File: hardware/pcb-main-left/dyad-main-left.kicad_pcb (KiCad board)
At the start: 2 copper layers, 149 x 120.7 mm, 129 parts, among them SW1 SW_Push, SW10 SW_Push, SW11 SW_Push, SW12 SW_Push, SW13 SW_Push, SW14 SW_Push, SW15 SW_Push, SW16 SW_Push, SW17 SW_Push, SW18 SW_Push, SW19 SW_Push, SW2 SW_Push, SW20 SW_Push, SW21 SW_Push, SW22 SW_Push, SW23 SW_Push, SW24 SW_Push, SW25 SW_Push, SW26 SW_Push, SW27 SW_Push, SW28 SW_Push, SW29 SW_Push, SW3 SW_Push, SW30 SW_Push, SW31 SW_Push, SW32 SW_Push, SW4 SW_Push, SW5 SW_Push, SW6 SW_Push, SW7 SW_Push, SW8 SW_Push, SW9 SW_Push

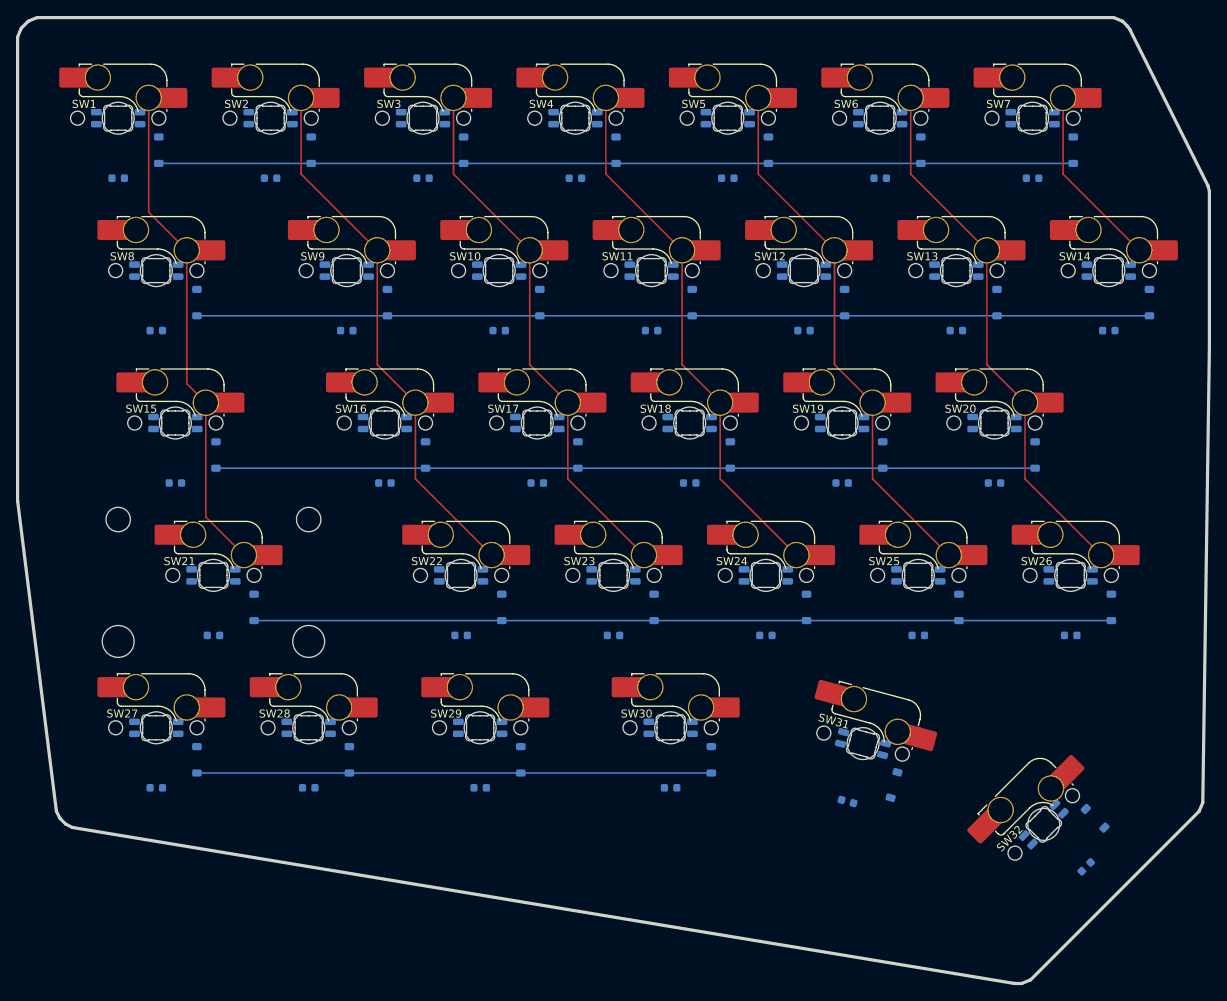
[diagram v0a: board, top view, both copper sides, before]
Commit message: Place switches on the back so hotswap sockets are on the underside
Caught in review: the sockets were on the same side as the switches.

marbastlib's hotswap footprint carries its socket pads on F.Cu and draws
its pin holes mirrored -- it is drawn as seen from underneath and must be
placed on the back. kbplacer defaults to front, so the sockets landed on
the switch side. Fixed with -s "SW{} 0 BACK"; stabilizers follow (they are
purely mechanical NPTH and X-symmetric, so flipping is a no-op for them).

Now every component is on the underside and switches insert from the top,
as a hotswap board should be. Verified: SW1's hotswap SMD pads are on
B.Cu, and the pin1->pin2 vector is (-6.35, 2.54), matching KiCad's stock
SW_Cherry_MX_1.00u_PCB. Absolute pad coordinates are not comparable
between the two libraries -- marbastlib's origin is the switch centre,
KiCad's is pin 1 -- so the vector is the valid test. An earlier claim in
this session that the geometry was mirrored wrongly was based on that bad
comparison and was itself wrong.

Also drops switch-to-diode routing failures, which were "no common layers
found" precisely because front-only SMD pads could not reach back-side
diodes.

DRC now runs and the boards are clearly a placement scaffold, not a
finished layout. Left: 1151 violations, 220 unconnected. Specific causes,
for the next pass:

- 128 hole_clearance: LEDs sit at the switch centre, 0.121 mm from the MX
  centre-post NPTH. The centre is where marbastlib puts its own combined
  MX+WS2812 footprint, but SK6812MINI-E is larger and fouls the post. LED
  offset needs rework.
- 128 copper_edge_clearance: the reverse-mount LED footprint's own cutout
  sits 0.35 mm from its pads against a 0.5 mm board rule. A board-setup
  constraint to relax, not a placement error.
- 192 shorting_items: diode pads overlapping switch through-holes after
  the flip, plus hotswap SMD pads left with no net, which points at an
  incomplete schematic-to-PCB netlist sync.
- Silk overlaps a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
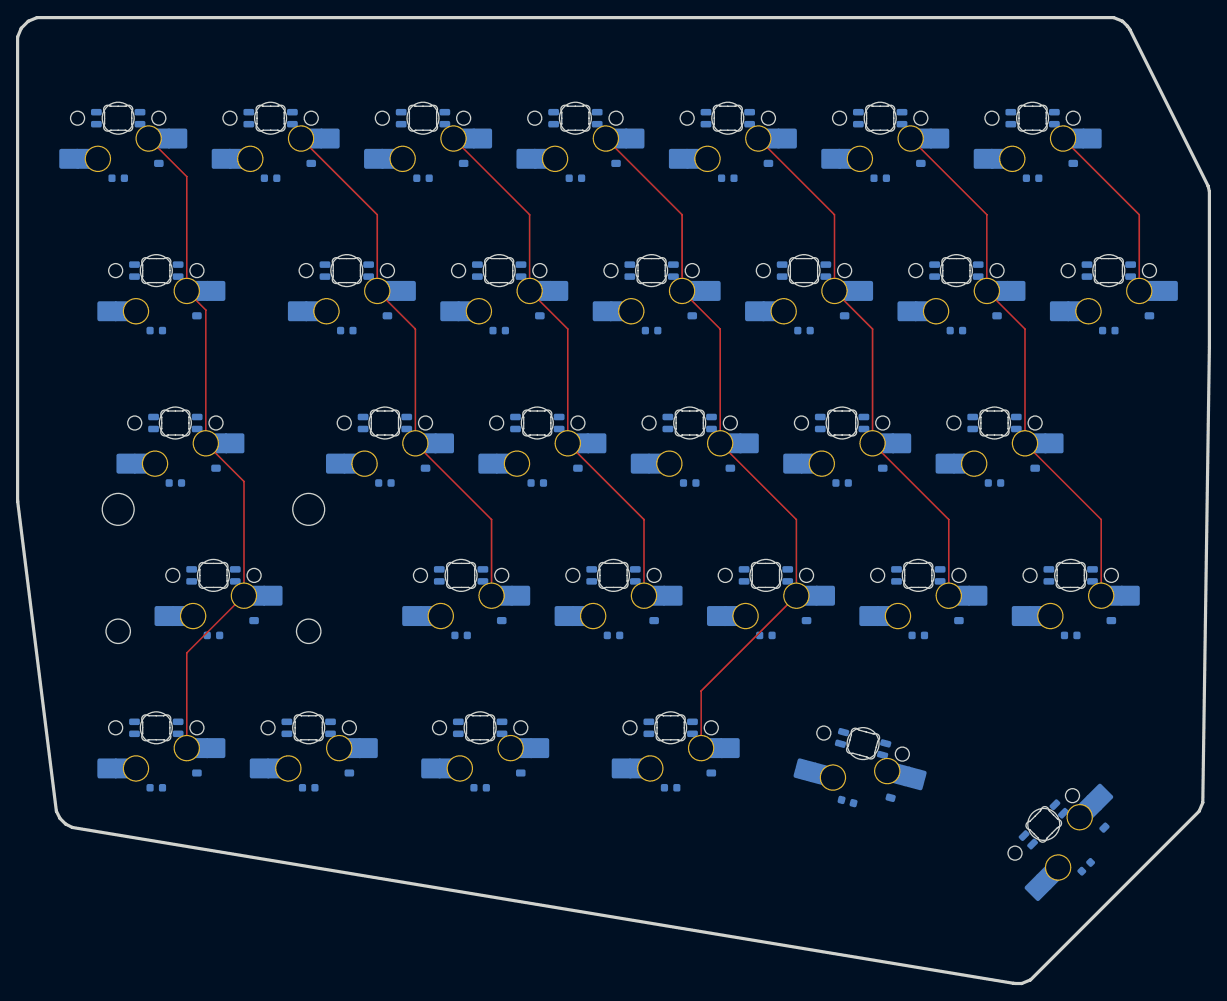
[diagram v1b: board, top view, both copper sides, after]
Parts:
- ST21, SW1, SW10, SW11, SW12, SW13, SW14, SW15, SW16, SW17, SW18, SW19, SW2, SW20, SW21, SW22, SW23, SW24, SW25, SW26, SW27, SW28, SW29, SW3, SW30, SW31, SW32, SW4, SW5, SW6, SW7, SW8, SW9: moved to B.Cu
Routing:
- net ROW1: track 119.1 -> 0.00 mm
- net ROW0: track 114.3 -> 0.00 mm
- net ROW3: track 107.2 -> 0.00 mm
- net ROW2: track 102.4 -> 0.00 mm
- net ROW4: track 64.3 -> 0.00 mm
- net COL3: track 67.0 -> 91.0 mm
- net COL0: track 62.1 -> 84.1 mm

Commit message: Fix LED offset and the placement errors it exposed
Working out the LED position turned up three further placement bugs.
Left board: 1151 -> 581 DRC violations, 220 -> 188 unconnected.

LED offset. ebastler's MX_SK6812MINI-E add-on -- a rear-mount SK6812MINI-E
for regular MX footprints -- puts its pads at y 4.33/5.83, centroid
(0, +5.08): 5.08 mm south of the switch centre, one fifth of an inch. Its
pad geometry matches KiCad's stock ReverseMount footprint almost exactly
(x +-2.6 vs +-2.73, same +-0.75 in y), so the maintained stock footprint
drops in at that offset. At the switch centre it fouled the MX centre-post
hole by 0.12 mm.

Switch rotation. The switches were 180 deg from convention: pins landed
SOUTH of centre, exactly where the LED goes. KiCad's stock MX footprint
puts them NORTH, at (+2.54,-5.08) and (-3.81,-2.54) relative to the
centre-post NPTH. An earlier commit asserted the geometry was correct on
the strength of the pin1->pin2 vector; that test cannot see this, because
a 180 deg rotation with swapped pin numbering preserves the vector.

Diode. kbplacer's default position assumes an unrotated switch, so it sat
beside the COLUMN pin, which the schematic does not wire it to. Moved
beside switch pin 2 and turned 180 deg so the anode rather than the ROW
pad faces the switch -- the ROW pad had been 0.035 mm from it.

Pad nets. marbastlib's hotswap footprint carries pad "1" three times, one
PTH and two SMD. kbplacer nets only one, so DRC saw each switch shorting
itself, 128 times per board. The generator now propagates nets across
same-numbered pads.

Also: min_copper_edge_clearance to 0.2 mm, since the reverse-mount LED
footprint's own light cutout sits 0.247 mm from its pads. Applied after
the board save, because saving rewrites the project file and silently
reverted it the first time.

Remaining, for a manual pass: roughly half the count is silkscreen
cosmetics and lib_footprint_issues (the libraries are referenced by
absolute path, so KiCad reports them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
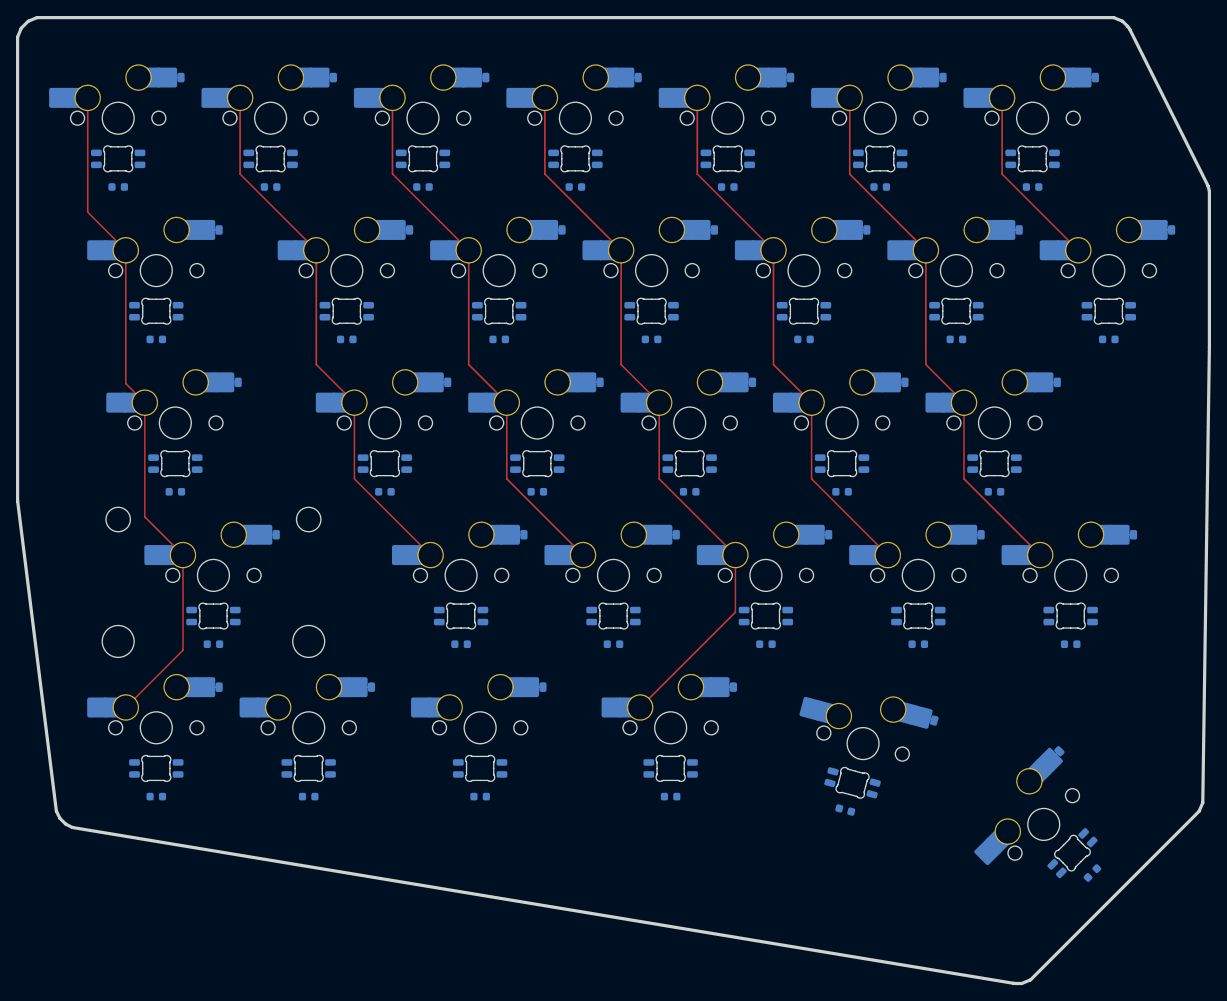
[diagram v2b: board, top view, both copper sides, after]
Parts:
- moved D32 9.15 mm to (154.6, 118.4), turned to 45 degrees
- moved D31 9.15 mm to (138.5, 113.0), turned to -15 degrees
- moved D1 9.15 mm to (44.3, 33.0), turned to 0 degrees
- moved D10 9.15 mm to (91.9, 52.1), turned to 0 degrees
- moved D11 9.15 mm to (111.0, 52.1), turned to 0 degrees
- moved D12 9.15 mm to (130.0, 52.1), turned to 0 degrees
- moved D14 9.15 mm to (168.1, 52.1), turned to 0 degrees
- moved D15 9.15 mm to (51.4, 71.1), turned to 0 degrees
- moved D16 9.15 mm to (77.6, 71.1), turned to 0 degrees
- moved D17 9.15 mm to (96.7, 71.1), turned to 0 degrees
- moved D18 9.15 mm to (115.7, 71.1), turned to 0 degrees
- moved D19 9.15 mm to (134.8, 71.1), turned to 0 degrees
- moved D2 9.15 mm to (63.4, 33.0), turned to 0 degrees
- moved D20 9.15 mm to (153.8, 71.1), turned to 0 degrees
- moved D21 9.15 mm to (56.2, 90.2), turned to 0 degrees
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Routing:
- net Net-(D25-A): track 0.00 -> 1.76 mm
- net Net-(D20-A): track 0.00 -> 1.76 mm
- net Net-(D14-A): track 0.00 -> 1.76 mm
- net Net-(D12-A): track 0.00 -> 1.76 mm
- net Net-(D28-A): track 0.00 -> 1.76 mm
- net Net-(D22-A): track 0.00 -> 1.76 mm
- net Net-(D18-A): track 0.00 -> 1.76 mm
- net Net-(D11-A): track 0.00 -> 1.76 mm
- net Net-(D10-A): track 0.00 -> 1.76 mm
- net Net-(D21-A): track 0.00 -> 1.76 mm
- net Net-(D1-A): track 0.00 -> 1.76 mm
- net Net-(D9-A): track 0.00 -> 1.76 mm
- net Net-(D5-A): track 0.00 -> 1.76 mm
- net Net-(D17-A): track 0.00 -> 1.76 mm
- net Net-(D8-A): track 0.00 -> 1.76 mm
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
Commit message: Move the diode clear of the hotswap socket pads
Caught in review: the diode sat on top of a hotswap socket pad.

Confirmed in board coordinates -- the pad-2 socket SMD pads are at
(4.34,-5.08) and (6.09,-5.08), and the diode was at (6.20,-5.08),
directly on them.

Moved to (+8.40,-5.08) rotated 90 deg, as suggested. Position was solved
rather than estimated: the closest placement to the pad-2 socket it has to
reach, with at least 0.4 mm clearance to every pad of the switch, LED, cap
and the four neighbouring key cells. Achieves 0.43 mm clearance and a
2.3 mm route. Verified the anode faces the switch and the cathode carries
the ROW net.

Left board 581 -> 225 DRC violations. Four categories went to zero:
shorting_items, solder_mask_bridge, clearance, copper_edge_clearance.

What remains is largely not electrical: 96 silk_over_copper, 33
lib_footprint_issues (the libraries are referenced by absolute path, so
KiCad reports them as unconfigured), 32 silk_overlap and 32
silk_edge_clearance. The substantive remainder is 32 courtyards_overlap
between each diode and its switch, one track crossing an LED cutout on the
right board, and 188 nets still unrouted including the angled thumb keys.

The 2.25u stabilised key still needs manual attention -- the stabiliser is
not represented in the clearance model, and is being handled by hand.

Co-Authored-By: Claude Opus 5 <noreply@anthropic.com>
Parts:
- moved D31 2.20 mm to (140.6, 113.5), turned to -105 degrees
- moved D32 2.20 mm to (156.1, 116.8), turned to -45 degrees
- moved D13 2.20 mm to (151.3, 52.1), turned to -90 degrees
- moved D19 2.20 mm to (137.0, 71.1), turned to -90 degrees
- moved D7 2.20 mm to (160.8, 33.0), turned to -90 degrees
- moved D1 2.20 mm to (46.5, 33.0), turned to -90 degrees
- moved D10 2.20 mm to (94.1, 52.1), turned to -90 degrees
- moved D11 2.20 mm to (113.2, 52.1), turned to -90 degrees
- moved D16 2.20 mm to (79.8, 71.1), turned to -90 degrees
- moved D17 2.20 mm to (98.9, 71.1), turned to -90 degrees
- moved D18 2.20 mm to (117.9, 71.1), turned to -90 degrees
- moved D21 2.20 mm to (58.4, 90.2), turned to -90 degrees
- moved D22 2.20 mm to (89.4, 90.2), turned to -90 degrees
- moved D24 2.20 mm to (127.5, 90.2), turned to -90 degrees
- moved D27 2.20 mm to (51.3, 109.2), turned to -90 degrees
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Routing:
- net Net-(D31-A): track 1.76 -> 2.99 mm
- net Net-(D32-A): track 1.76 -> 2.99 mm
- net Net-(D30-A): track 1.76 -> 2.99 mm
- net Net-(D29-A): track 1.76 -> 2.99 mm
- net Net-(D26-A): track 1.76 -> 2.99 mm
- net Net-(D24-A): track 1.76 -> 2.99 mm
- net Net-(D13-A): track 1.76 -> 2.99 mm
- net Net-(D7-A): track 1.76 -> 2.99 mm
- net Net-(D6-A): track 1.76 -> 2.99 mm
- net Net-(D4-A): track 1.76 -> 2.99 mm
- net Net-(D8-A): track 1.76 -> 2.99 mm
- net Net-(D27-A): track 1.76 -> 2.99 mm
- net Net-(D9-A): track 1.76 -> 2.99 mm
- net Net-(D23-A): track 1.76 -> 2.99 mm
- net Net-(D19-A): track 1.76 -> 2.99 mm
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
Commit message: Export main PCB outlines for the case
hardware/export_outlines.py writes, per half, into hardware/outlines/:
a perimeter-only DXF for CAD import, the vertices as JSON for scripted
CAD, the interior cutouts separately, and a STEP of the populated board
as the 3D fit reference WORKFLOW section 5 calls for.

Left 148.97 x 120.74 mm, 23 vertices. Right 167.21 x 120.74 mm, 25
vertices.

The perimeter comes from the board's computed polygon outlines rather
than the raw Edge.Cuts layer, because the reverse-mount LED footprint
cuts its own light hole and Edge.Cuts therefore carries ~640 extra loops
per board that are nothing to do with the case. Those are written out
separately rather than silently dropped. DXF verified by re-parsing it
and diffing against the JSON: max delta 0.0005 mm.

Also records the pod centre in PCB coordinates, which the case needs and
which is not otherwise derivable -- the knob module is a separate PCB, so
the pod does not appear on the main board at all. Left (197.17, 108.58),
right (2.86, 108.58).

That exposes something for the case to resolve: both pod centres lie
OUTSIDE their main board, and the 50 mm ring overhangs the board edge by
2.3 mm on the left and 1.5 mm on the right. The two PCBs therefore
overlap in plan view and must be separated in Z, or the main outline
needs a notch. Flagged in interface.yaml for G3.

WORKFLOW section 5 gains a direction note: it assumes the case owns the
outline, but today the outline flows KiCad -> CAD because kbplacer
generated it. Ownership should flip at G3, and only one side owns it at
a time.

Co-Authored-By: Claude Opus 5 <noreply@anthropic.com>
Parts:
- moved D21 3.82 mm to (58.4, 86.3)
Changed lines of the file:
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@@
 	(footprint "Diode_SMD:D_SOD-123"
 		(layer "B.Cu")
-		(at 58.40625 90.170001 -90)
+		(at 58.40625 86.35 -90)
 		(descr "SOD-123")
 		(tags "SOD-123")

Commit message: Regenerate both main PCBs with hierarchical sheet bundling
Re-ran generate_main_pcbs.py so the --bundle-strategy hierarchical change
takes effect. Each half now has a proper root sheet:

  dyad-main-<half>.kicad_sch             0 symbols, 2 child sheet refs
  dyad-main-<half>-key-matrix.kicad_sch  65 / 74 symbols   (new file)
  dyad-main-<half>-led-chain.kicad_sch   130 / 150 symbols

The key-matrix sheet is new: flat bundling put those symbols in the root
itself, hierarchical moves them into their own child sheet.

Schematic parity is the point of the exercise:

              before              after
  main-left   64 Extra footprint  0
  main-right  74 Extra footprint  0

Every LED and decoupling capacitor now resolves to a symbol. The parity
counts happen to be unchanged (98 and 111) but the composition is entirely
different -- what remains is cosmetic field sync (Sim.Device, Description
and Datasheet empty on the PCB side), not missing structure.

min_copper_edge_clearance is 0.2 on both, so _relax_edge_clearance ran, and
the fp-lib-table files added earlier were preserved, so lib_footprint_issues
stays at zero.

Known, unchanged by this commit:
  - COL6 vs LED14's cutout is back at 0.036 mm on main-right, identical to
    before -- kbplacer re-routes it the same way every time, which is why
    the hand fix in e7043c7 was always going to be temporary.
  - The 2.25u stabilised key still falls back to a 1.0u footprint.
  - Four rotated thumb/pod pairs per half remain unrouted ("Could not route
    pads when parent footprints not rotated the same").

Co-Authored-By: Claude Opus 5 <noreply@anthropic.com>
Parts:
- moved D21 3.82 mm to (58.4, 90.2)
